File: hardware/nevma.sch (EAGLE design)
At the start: 9 parts, among them J1 USB_A_PTH_MALE, U1 TINY85-20-DIP

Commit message: Correct resistor value
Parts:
- R2: value 68Ω -> 1.5KΩ
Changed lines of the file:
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@@
 <part name="R1" library="rcl" library_urn="urn:adsk.eagle:library:334" deviceset="R-US_" device="0204/7" package3d_urn="urn:adsk.eagle:package:23498/1" value="4.7KΩ"/>
 <part name="SUPPLY3" library="SparkFun-PowerSymbols" library_urn="urn:adsk.eagle:library:530" deviceset="VCC" device=""/>
-<part name="R2" library="rcl" library_urn="urn:adsk.eagle:library:334" deviceset="R-US_" device="0204/7" package3d_urn="urn:adsk.eagle:package:23498/1" value="68Ω"/>
+<part name="R2" library="rcl" library_urn="urn:adsk.eagle:library:334" deviceset="R-US_" device="0204/7" package3d_urn="urn:adsk.eagle:package:23498/1" value="1.5KΩ"/>
 </parts>
 <sheets>

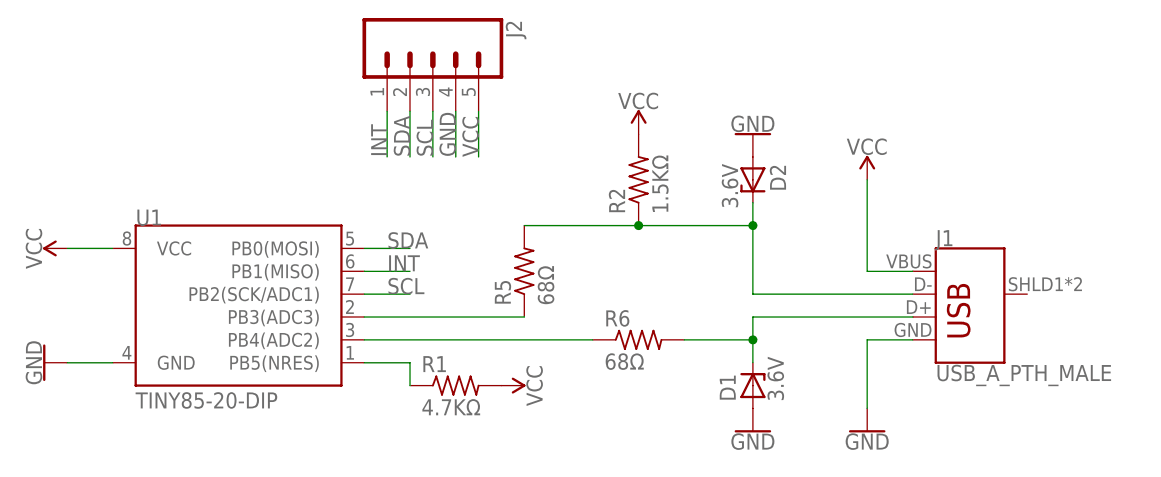
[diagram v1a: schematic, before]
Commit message: New concept based on atmega32u4 board
HW rev. 2
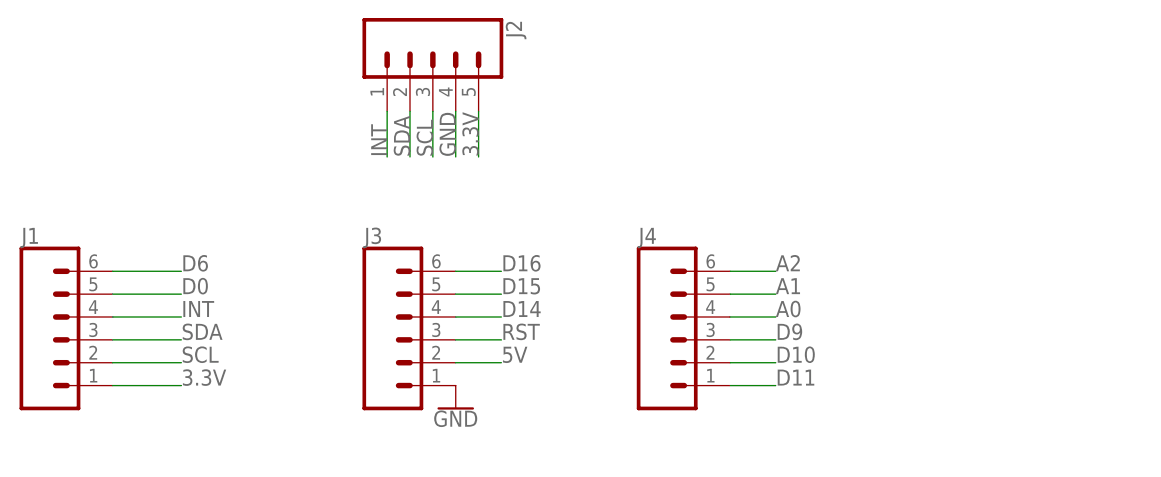
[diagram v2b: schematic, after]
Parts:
- removed D1, D2: 3.6V, diode:ZENER-DIODEDO35Z10
- removed R1: 4.7KΩ, rcl:R-US_0204/7
- removed R2: 1.5KΩ, rcl:R-US_0204/7
- removed R5, R6: 68Ω, rcl:R-US_0204/7
- removed U1: TINY85-20-DIP, SparkFun-Retired:ATTINY45TINY85-20-DIP
- added J3, J4: (no value), SparkFun-Connectors:CONN_06LOCK
- J1: value USB_A_PTH_MALE -> (none); device SparkFun-Connectors:USB_A_PTH_MALE -> SparkFun-Connectors:CONN_06LOCK
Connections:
- removed net N$1: R6.1, U1.PB4(ADC2)
- removed net N$2: R5.1, U1.PB3(ADC3)
- removed net N$3: D2.C, J1.D-, R2.1, R5.2
- removed net N$4: D1.C, J1.D+, R6.2
- removed net VCC: J1.VBUS, J2.5, R1.2, R2.2, U1.VCC
- new net 3.3V: J1.1, J2.5
- new net 5V: J3.2
- new net A0: J4.4
- new net A1: J4.5
- new net A2: J4.6
- new net D0: J1.5
- new net D10: J4.2
- new net D11: J4.1
- new net D14: J3.4
- new net D15: J3.5
- new net D16: J3.6
- new net D6: J1.6
- new net D9: J4.3
- net GND: now also J3.1; no longer D1.A, D2.A, J1.GND, U1.GND
- net INT: now also J1.4; no longer U1.PB1(MISO)
- net RST: now also J3.3; no longer R1.1, U1.PB5(NRES)
- net SCL: now also J1.2; no longer U1.PB2(SCK/ADC1)
- net SDA: now also J1.3; no longer U1.PB0(MOSI)
